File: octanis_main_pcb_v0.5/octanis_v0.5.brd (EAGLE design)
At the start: 80 x 48 mm, 103 parts, among them IC1 BME280, IC2 BNO055A, Q1 32.768kHz, Q2 32.768kHz, U1 TPS61232, U10 INA213, U11 INA213, U12 INA213, U2 DRV8836DSSR, U3 DRV8836DSSR, U4 MSP432, U5 SST25VF064C, U6 DRV8836DSSR, U7 DRV8836DSSR, U8 MAX6001SOT-23, U9 INA213

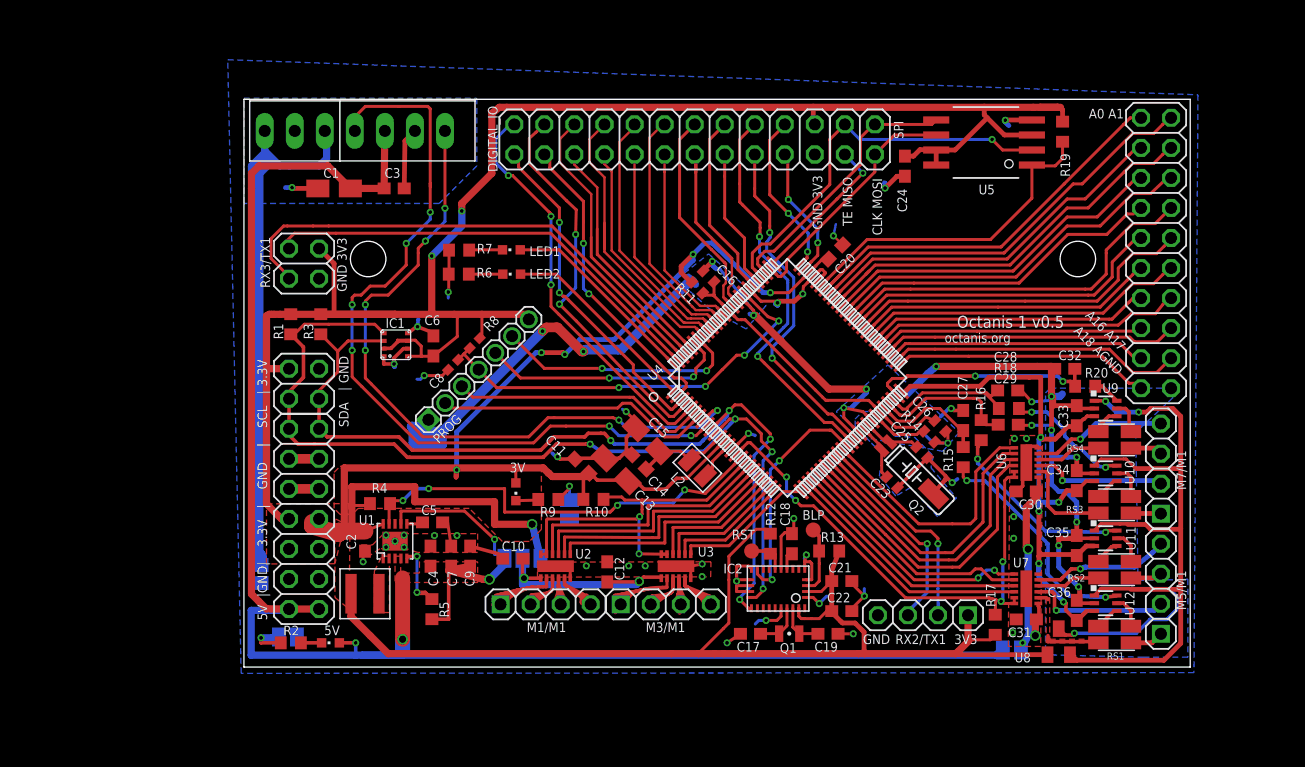
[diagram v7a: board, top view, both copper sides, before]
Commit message: added RN2483 LoRa module, separated 3v supply for motors and 5V converter from main circuit supply. *
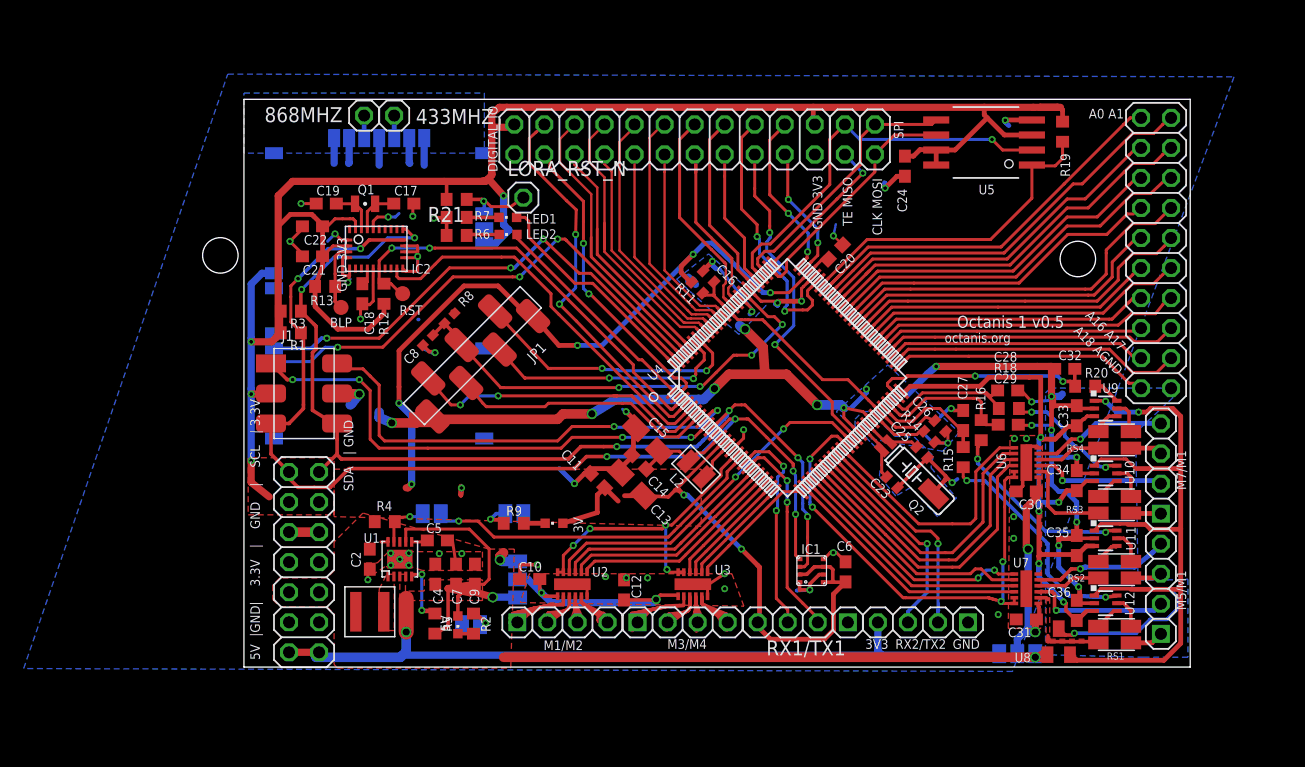
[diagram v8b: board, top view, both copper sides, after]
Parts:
- removed C1: 10u, rcl:A/3216-18R
- removed C3: 100n, rcl:C0603
- removed M1/M1, M3/M1, RX2/TX1: (no value), pinhead-2:1X04-S
- removed MOT_J, RF_J: (no value), jumper:SJ
- removed PROG: (no value), Headerlibrary:1:07X2MM
- removed R10, R17: 10k, rcl:R0603
- removed RX3/TX1: (no value), pinhead:2X02
- removed U$1: HX1EXTERNALMOUNT, Octanis1:HX1_EXT
- added 433MHZ, 868MHZ, LORA_RST_N: (no value), Headerlibrary:1X01
- added J1: (no value), Seeed-OPL-Connector:H2X3-SMD-2.54
- added M1/M2, M3/M4, RX1/TX1, RX2/TX2: (no value), pinhead-2:1X04-S
- added MOT_J1: (no value), jumper:SJ
- added R21: 100k, rcl:R0603
- added U13: RN2483, Octanis1:RN2483
- added VMOT_SEL2: 3V3 V_Motor 5V, jumper:SJ_2
- JP1: device pinhead:2X02 -> Headerlibrary:1X7SMD
- R12, R13: value 10k -> 100k
- moved C19 55.9 mm to (6.96, 40.2), turned to 180 degrees
- moved C22 55.3 mm to (5.79, 38.3), turned to 180 degrees
- moved C21 52.5 mm to (5.79, 35.7), turned to 180 degrees
- moved Q1 51.1 mm to (10.2, 40.2), turned to 180 degrees
- moved R13 48.1 mm to (6.86, 33.2), turned to 180 degrees
- moved C17 46.7 mm to (13.5, 40.2), turned to 0 degrees
- moved IC2 44.5 mm to (11.2, 36.4), turned to 90 degrees
- moved BLP 44.1 mm to (8.21, 31.4), turned to 180 degrees
- moved C18 42.0 mm to (10.0, 32.6), turned to 90 degrees
- moved IC1 40.0 mm to (48.0, 9.15)
- moved C6 39.7 mm to (50.9, 9.05)
- moved R12 38.9 mm to (11.8, 32.6), turned to 90 degrees
- moved RST 36.7 mm to (13.4, 32.6), turned to 180 degrees
- moved R2 15.5 mm to (19.4, 4.67), turned to 270 degrees
- moved LED_J101 15.5 mm to (19.2, 4.59), turned to 180 degrees
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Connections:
- removed net HX1_DATA: U$1.TXD, U4.8
- removed net HX1_EN: U$1.EN, U4.9
- removed net P1.1: DIGITAL_IO.21, U4.5
- removed net P10.3: DIGITAL_IO.22, U4.3
- removed net P3.6: DIGITAL_IO.5, U4.38
- removed net RFGND: C1.-, C3.2, RF_J.2, U$1.0V, U$1.RFGND, U$1.RFGND2
- new net 3V3_MODULE2: C2.1, JP2.10, JP2.9, L1.P$1, R4.2, U1.10, U8.1, VMOT_SEL.1, VMOT_SEL2.1
- new net ANT433: 433MHZ.1, U13.P$25
- new net ANT868: 868MHZ.1, U13.P$23
- new net EXT_LIGHTNING_INT: J1.6, U4.8
- new net EXT_UV_EN: J1.1, U4.9
- new net LORA_RST_N: LORA_RST_N.1, R21.1, U13.P$32
- new net N$20: MOT_J1.1, R4.1, U1.9
- new net P5.7: DIGITAL_IO.5, U4.71
- new net RX1: RX1/TX1.3, U4.18
- new net TX1: RX1/TX1.2, U4.19
- net +3V3: now also DIGITAL_IO.21, J1.2, JP1.7, JP2.3, JP2.4, R21.2, RX1/TX1.4, U13.P$12, U13.P$34; no longer C2.1, JP1.1, JP2.10, JP2.7, JP2.8, JP2.9, L1.P$1, PROG.7, R10.2, R17.2, R4.2, RX2/TX1.1, RX3/TX1.3, U1.10, U8.1, VMOT_SEL.1
- net +5V: now also RX2/TX2.4, VMOT_SEL2.3; no longer C1.+, C3.1, MOT_J.2, U$1.VCC
- net 5VEN: now also MOT_J1.2; no longer R4.1, U1.9
- net ACCEL_INT: now also U4.5; no longer U4.37
- net ACCEL_N_RST: now also U4.3
- net GND: now also DIGITAL_IO.22, J1.5, JP1.1, JP2.7, JP2.8, RX1/TX1.1, RX2/TX2.1, U13.P$1, U13.P$11, U13.P$20, U13.P$21, U13.P$22, U13.P$24, U13.P$26, U13.P$27, U13.P$28, U13.P$33, U13.P$41, U13.P$47, U13.P$8; no longer JP1.2, JP2.3, JP2.4, PROG.1, RF_J.1, RX2/TX1.4, RX3/TX1.1, U4.71
- net M1234SLEEP: now also U4.16; no longer R10.1, U4.18
- net M1IN1: now also U4.38; no longer U4.19
- net M5678SLEEP: now also U4.37; no longer R17.1, U4.16
- net N$13: now also M3/M4.1; no longer M3/M1.1
- net N$39: now also M3/M4.2; no longer M3/M1.2
- net N$40: now also M3/M4.3; no longer M3/M1.3
- net N$41: now also M3/M4.4; no longer M3/M1.4
- net N$49: now also M1/M2.1; no longer M1/M1.1
- net N$50: now also M1/M2.2; no longer M1/M1.2
- net N$51: now also M1/M2.3; no longer M1/M1.3
- net N$52: now also M1/M2.4; no longer M1/M1.4
- net N$76: now also JP1.6; no longer PROG.6
- net N$77: now also JP1.5; no longer PROG.5
- net RST_N: now also JP1.4; no longer PROG.4
- net RX0: now also JP1.2; no longer PROG.2
- net RX2: now also RX2/TX2.3; no longer RX2/TX1.3
- net RX3: now also U13.P$6; no longer RX3/TX1.2
- net SCL: now also J1.3; no longer JP1.3
- net SDA: now also J1.4; no longer JP1.4
- net TX0: now also JP1.3; no longer PROG.3
- net TX2: now also RX2/TX2.2; no longer RX2/TX1.2
- net TX3: now also U13.P$7; no longer RX3/TX1.4
- net V_MOTOR2: now also VMOT_SEL2.2; no longer MOT_J.1
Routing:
- net +3V3: track 385.0 -> 294.4 mm, vias 8 -> 12
- net +5V: track 168.6 -> 97.1 mm, vias 4 -> 2
- net HX1_EN: track 68.4 -> 0.00 mm, vias 6 -> 0
- net HX1_DATA: track 59.7 -> 0.00 mm, vias 6 -> 0
- net RFGND: track 54.9 -> 0.00 mm, vias 1 -> 0
- net 3V3_MODULE2: track 0.00 -> 49.7 mm, vias 0 -> 2
- net EXT_UV_EN: track 0.00 -> 43.1 mm, vias 0 -> 4
- net EXT_LIGHTNING_INT: track 0.00 -> 40.0 mm, vias 0 -> 2
- net P1.1: track 34.8 -> 0.00 mm, vias 3 -> 0
- net P3.6: track 33.8 -> 0.00 mm, vias 2 -> 0
- net ACCEL_N_RST: track 3.28 -> 36.6 mm, vias 0 -> 2
- net P10.3: track 28.5 -> 0.00 mm, vias 2 -> 0
- net P5.7: track 0.00 -> 23.1 mm, vias 0 -> 2
- net RX1: track 0.00 -> 18.0 mm, vias 0 -> 2
- net TX1: track 0.00 -> 17.4 mm, vias 0 -> 2
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- added copper zone on layer 1, net 3V3_MODULE2
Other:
- board text added: "3V3 GND"
